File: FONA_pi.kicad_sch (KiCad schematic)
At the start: 6 parts, among them J1 Conn_01x20_Socket, J2 Conn_02x20_Odd_Even, J3 Conn_01x20_Socket, J5 Conn_01x20_Socket, J6 Conn_01x20_Socket, J8 Conn_01x20_Socket

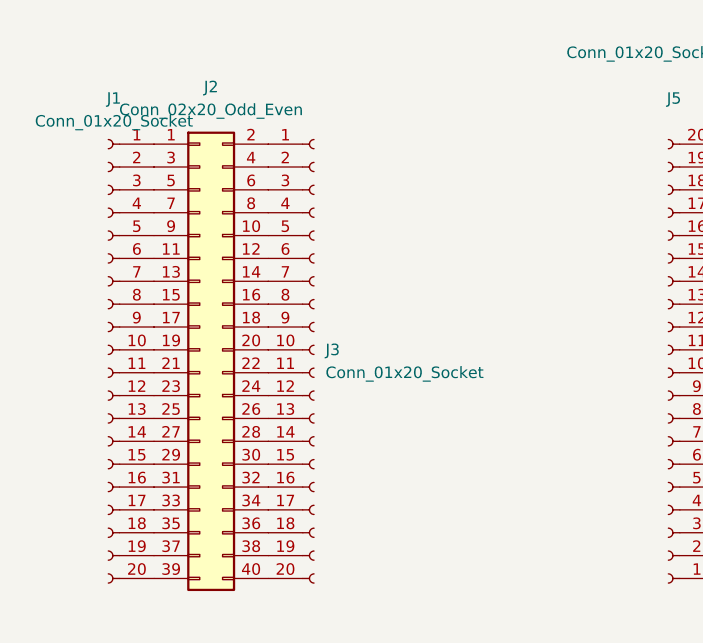
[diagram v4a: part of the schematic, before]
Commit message: Added more rows of holes to connect to Pi
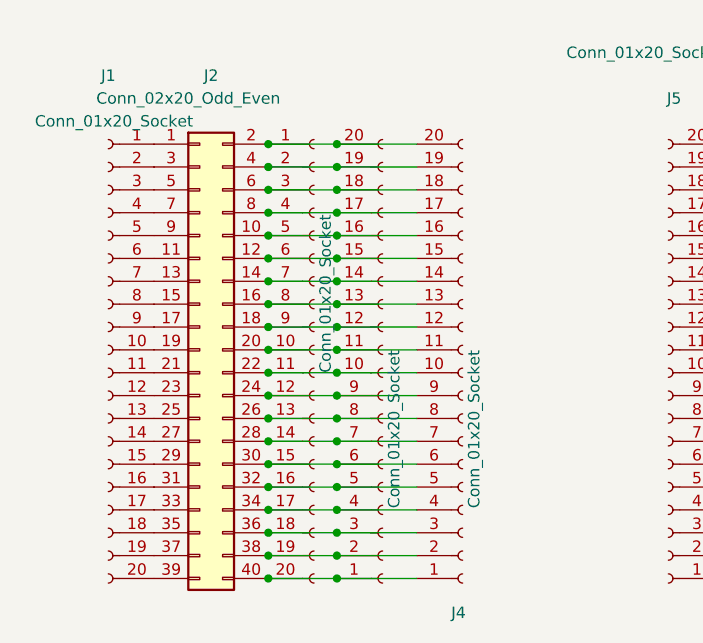
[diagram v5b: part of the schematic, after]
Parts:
- added J4, J7: Conn_01x20_Socket, Connector_PinHeader_2.54mm:PinHeader_1x20_P2.54mm_Vertical, symbol Connector:Conn_01x20_Socket
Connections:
- net at J2.10 (Pin_10), J3.5 (Pin_5): now also J4.16 (Pin_16), J7.16 (Pin_16)
- net at J2.12 (Pin_12), J3.6 (Pin_6): now also J4.15 (Pin_15), J7.15 (Pin_15)
- net at J2.14 (Pin_14), J3.7 (Pin_7): now also J4.14 (Pin_14), J7.14 (Pin_14)
- net at J2.16 (Pin_16), J3.8 (Pin_8): now also J4.13 (Pin_13), J7.13 (Pin_13)
- net at J2.18 (Pin_18), J3.9 (Pin_9): now also J4.12 (Pin_12), J7.12 (Pin_12)
- net at J2.2 (Pin_2), J3.1 (Pin_1): now also J4.20 (Pin_20), J7.20 (Pin_20)
- net at J2.20 (Pin_20), J3.10 (Pin_10): now also J4.11 (Pin_11), J7.11 (Pin_11)
- net at J2.22 (Pin_22), J3.11 (Pin_11): now also J4.10 (Pin_10), J7.10 (Pin_10)
- net at J2.24 (Pin_24), J3.12 (Pin_12): now also J4.9 (Pin_9), J7.9 (Pin_9)
- net at J2.26 (Pin_26), J3.13 (Pin_13): now also J4.8 (Pin_8), J7.8 (Pin_8)
- net at J2.28 (Pin_28), J3.14 (Pin_14): now also J4.7 (Pin_7), J7.7 (Pin_7)
- net at J2.30 (Pin_30), J3.15 (Pin_15): now also J4.6 (Pin_6), J7.6 (Pin_6)
- net at J2.32 (Pin_32), J3.16 (Pin_16): now also J4.5 (Pin_5), J7.5 (Pin_5)
- net at J2.34 (Pin_34), J3.17 (Pin_17): now also J4.4 (Pin_4), J7.4 (Pin_4)
- net at J2.36 (Pin_36), J3.18 (Pin_18): now also J4.3 (Pin_3), J7.3 (Pin_3)
- net at J2.38 (Pin_38), J3.19 (Pin_19): now also J4.2 (Pin_2), J7.2 (Pin_2)
- net at J2.4 (Pin_4), J3.2 (Pin_2): now also J4.19 (Pin_19), J7.19 (Pin_19)
- net at J2.40 (Pin_40), J3.20 (Pin_20): now also J4.1 (Pin_1), J7.1 (Pin_1)
- net at J2.6 (Pin_6), J3.3 (Pin_3): now also J4.18 (Pin_18), J7.18 (Pin_18)
- net at J2.8 (Pin_8), J3.4 (Pin_4): now also J4.17 (Pin_17), J7.17 (Pin_17)

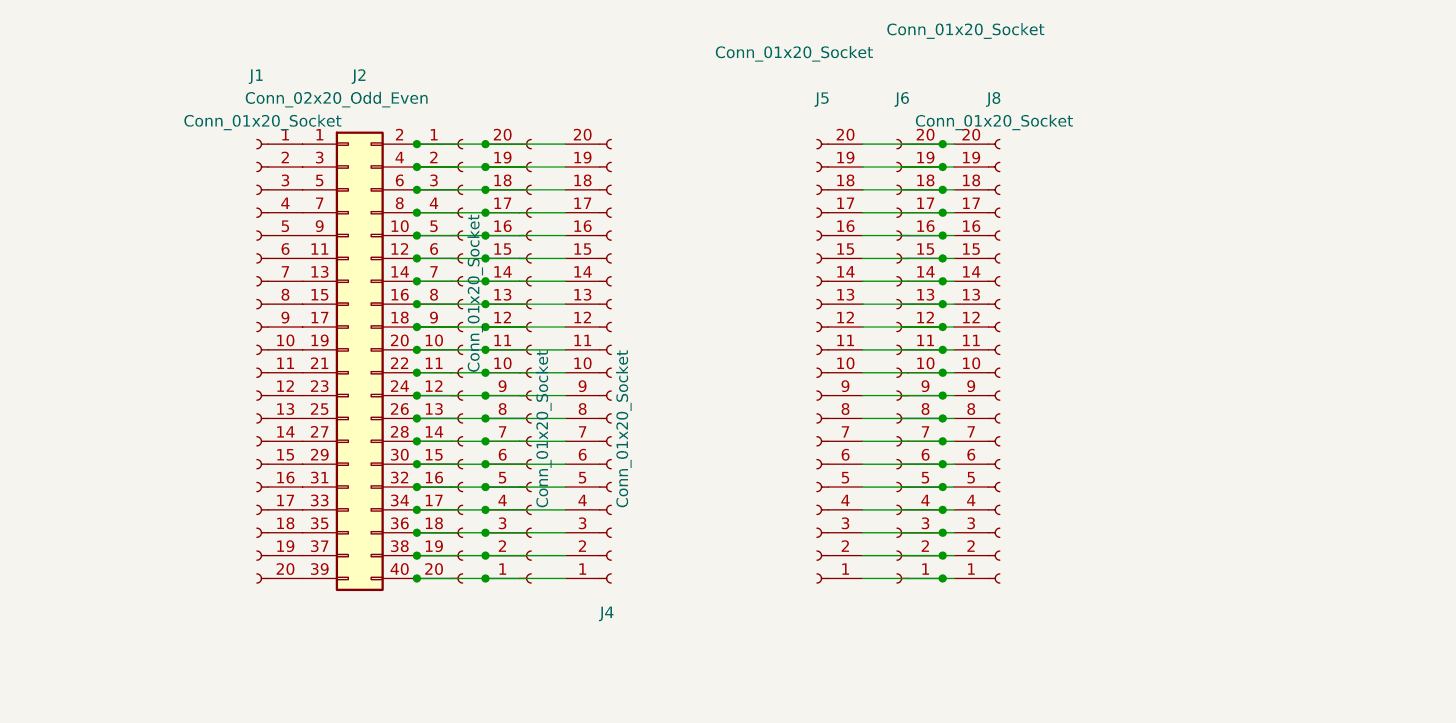
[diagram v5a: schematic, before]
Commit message: flipped RPi orientation on schematic.  Added three 3mm LEDs with resistors on sch and pcb.  Wired up with traces
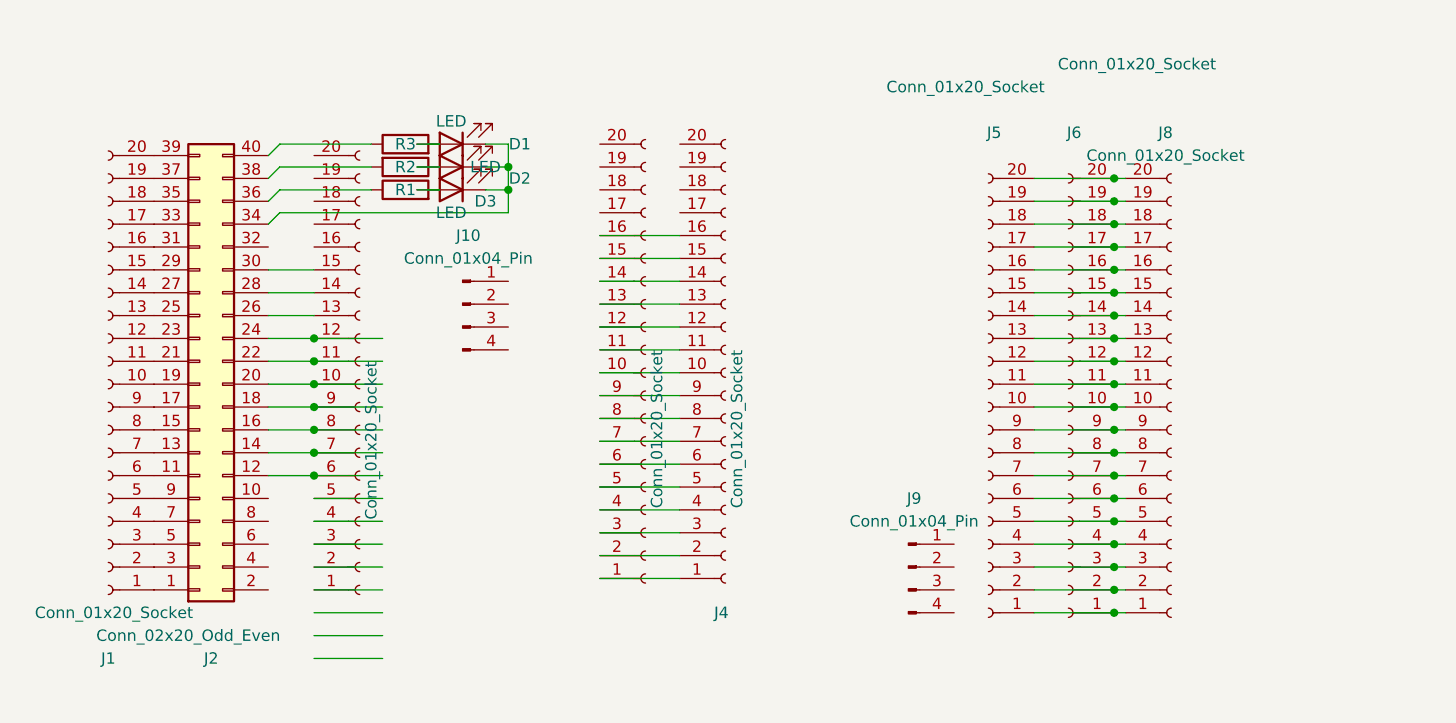
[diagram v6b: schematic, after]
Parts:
- added D1, D2, D3: LED, LED_THT:LED_D3.0mm, symbol Device:LED
- added J10, J9: Conn_01x04_Pin, symbol Connector:Conn_01x04_Pin
- added R1, R2, R3: R, Resistor_THT:R_Axial_DIN0207_L6.3mm_D2.5mm_P7.62mm_Horizontal, symbol Device:R
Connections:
- net at J4.1 (Pin_1), J7.1 (Pin_1): no longer J2.40 (Pin_40), J3.20 (Pin_20)
- net at J4.10 (Pin_10), J7.10 (Pin_10): no longer J2.22 (Pin_22), J3.11 (Pin_11)
- net at J4.11 (Pin_11), J7.11 (Pin_11): no longer J2.20 (Pin_20), J3.10 (Pin_10)
- net at J4.12 (Pin_12), J7.12 (Pin_12): no longer J2.18 (Pin_18), J3.9 (Pin_9)
- net at J4.13 (Pin_13), J7.13 (Pin_13): no longer J2.16 (Pin_16), J3.8 (Pin_8)
- net at J4.14 (Pin_14), J7.14 (Pin_14): no longer J2.14 (Pin_14), J3.7 (Pin_7)
- net at J4.15 (Pin_15), J7.15 (Pin_15): no longer J2.12 (Pin_12), J3.6 (Pin_6)
- net at J4.16 (Pin_16), J7.16 (Pin_16): no longer J2.10 (Pin_10), J3.5 (Pin_5)
- net at J4.2 (Pin_2), J7.2 (Pin_2): no longer J2.38 (Pin_38), J3.19 (Pin_19)
- net at J4.3 (Pin_3), J7.3 (Pin_3): no longer J2.36 (Pin_36), J3.18 (Pin_18)
- net at J4.4 (Pin_4), J7.4 (Pin_4): no longer J2.34 (Pin_34), J3.17 (Pin_17)
- net at J4.5 (Pin_5), J7.5 (Pin_5): no longer J2.32 (Pin_32), J3.16 (Pin_16)
- net at J4.6 (Pin_6), J7.6 (Pin_6): no longer J2.30 (Pin_30), J3.15 (Pin_15)
- net at J4.7 (Pin_7), J7.7 (Pin_7): no longer J2.28 (Pin_28), J3.14 (Pin_14)
- net at J4.8 (Pin_8), J7.8 (Pin_8): no longer J2.26 (Pin_26), J3.13 (Pin_13)
- net at J4.9 (Pin_9), J7.9 (Pin_9): no longer J2.24 (Pin_24), J3.12 (Pin_12)
- new net: D2.2 (A), R2.1
- new net: J2.38 (Pin_38), R2.2
- new net: J2.12 (Pin_12), J3.6 (Pin_6)
- new net: J2.14 (Pin_14), J3.7 (Pin_7)
- new net: J2.16 (Pin_16), J3.8 (Pin_8)
- new net: J2.18 (Pin_18), J3.9 (Pin_9)
- new net: J2.20 (Pin_20), J3.10 (Pin_10)
- new net: J2.22 (Pin_22), J3.11 (Pin_11)
- new net: J2.24 (Pin_24), J3.12 (Pin_12)
- new net: J2.26 (Pin_26), J3.13 (Pin_13)
- new net: J2.28 (Pin_28), J3.14 (Pin_14)
- new net: J2.30 (Pin_30), J3.15 (Pin_15)
- new net: D1.1 (K), D2.1 (K), D3.1 (K), J2.34 (Pin_34)
- new net: J2.36 (Pin_36), R1.1
- new net: J2.40 (Pin_40), R3.1
- new net: D1.2 (A), R3.2
- new net: D3.2 (A), R1.2
- now unconnected: J2.2 (Pin_2), J2.4 (Pin_4), J2.6 (Pin_6), J2.8 (Pin_8), J3.1 (Pin_1), J3.2 (Pin_2), J3.3 (Pin_3), J3.4 (Pin_4), J4.17 (Pin_17), J4.18 (Pin_18), J4.19 (Pin_19), J4.20 (Pin_20), J7.17 (Pin_17), J7.18 (Pin_18), J7.19 (Pin_19), J7.20 (Pin_20)
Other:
- moved on the sheet: J1, J2, J4, J5, J6, J8

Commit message: Hooked up JST-XH connectors, resistors
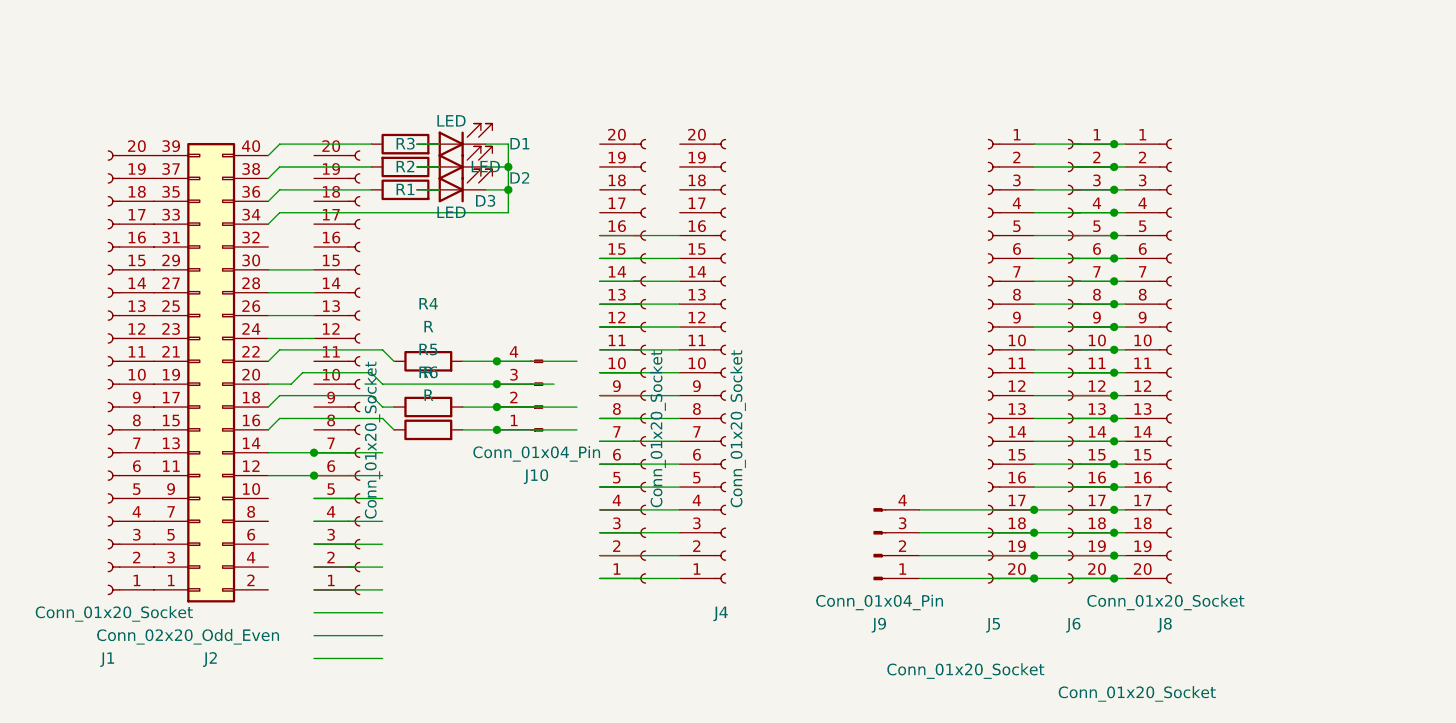
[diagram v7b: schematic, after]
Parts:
- added R4, R5, R6: R, Resistor_THT:R_Axial_DIN0207_L6.3mm_D2.5mm_P7.62mm_Horizontal, symbol Device:R
- J10, J9: footprint (none) -> Connector_JST:JST_XH_B4B-XH-A_1x04_P2.50mm_Vertical
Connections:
- net at J5.17 (Pin_17), J6.17 (Pin_17), J8.17 (Pin_17): now also J9.4 (Pin_4)
- net at J5.18 (Pin_18), J6.18 (Pin_18), J8.18 (Pin_18): now also J9.3 (Pin_3)
- net at J5.19 (Pin_19), J6.19 (Pin_19), J8.19 (Pin_19): now also J9.2 (Pin_2)
- net at J5.20 (Pin_20), J6.20 (Pin_20), J8.20 (Pin_20): now also J9.1 (Pin_1)
- net at J2.16 (Pin_16): now also R6.1; no longer J3.8 (Pin_8)
- net at J2.18 (Pin_18): now also R5.1; no longer J3.9 (Pin_9)
- net at J2.20 (Pin_20): now also J10.3 (Pin_3); no longer J3.10 (Pin_10)
- net at J2.22 (Pin_22): now also R4.1; no longer J3.11 (Pin_11)
- net at J10.1 (Pin_1): now also R6.2
- net at J10.2 (Pin_2): now also R5.2
- net at J10.4 (Pin_4): now also R4.2
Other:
- moved on the sheet: J10, J5, J6, J8, J9

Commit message: Flipped RPi pins.  Added silkscreen labels for pins.  Connected wires and tracks
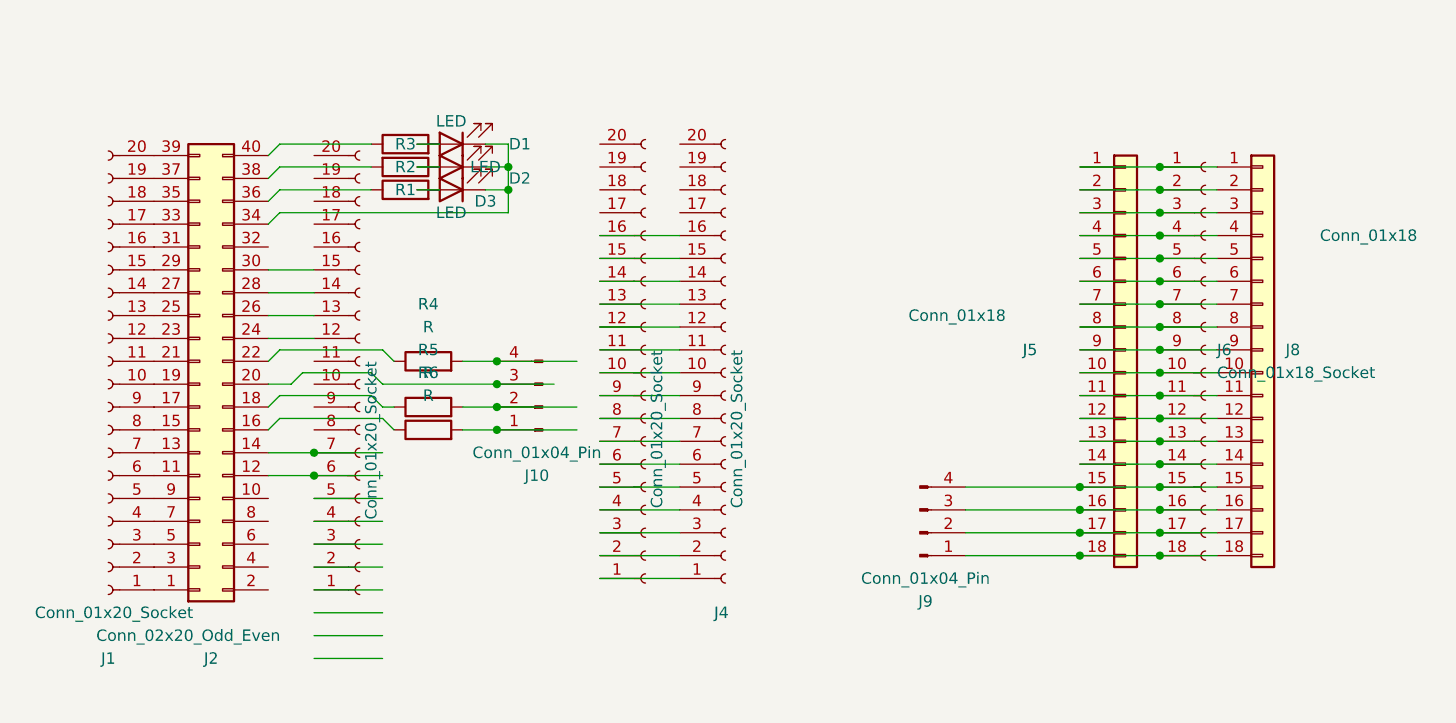
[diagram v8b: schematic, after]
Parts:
- removed J5, J6, J8: Conn_01x20_Socket, Connector_PinSocket_2.54mm:PinSocket_1x20_P2.54mm_Vertical, symbol Connector:Conn_01x20_Socket
- added J5, J8: Conn_01x18, Connector_PinSocket_2.54mm:PinSocket_1x18_P2.54mm_Vertical, symbol Connector_Generic:Conn_01x18
- added J6: Conn_01x18_Socket, Connector_PinSocket_2.54mm:PinSocket_1x18_P2.54mm_Vertical, symbol Connector:Conn_01x18_Socket
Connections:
- net at J9.4 (Pin_4): now also J5.15 (Pin_15), J6.15 (Pin_15), J8.15 (Pin_15)
- net at J9.3 (Pin_3): now also J5.16 (Pin_16), J6.16 (Pin_16), J8.16 (Pin_16)
- net at J9.2 (Pin_2): now also J5.17 (Pin_17), J6.17 (Pin_17), J8.17 (Pin_17)
- net at J9.1 (Pin_1): now also J5.18 (Pin_18), J6.18 (Pin_18), J8.18 (Pin_18)
- new net: J5.1 (Pin_1), J6.1 (Pin_1), J8.1 (Pin_1)
- new net: J5.10 (Pin_10), J6.10 (Pin_10), J8.10 (Pin_10)
- new net: J5.11 (Pin_11), J6.11 (Pin_11), J8.11 (Pin_11)
- new net: J5.12 (Pin_12), J6.12 (Pin_12), J8.12 (Pin_12)
- new net: J5.13 (Pin_13), J6.13 (Pin_13), J8.13 (Pin_13)
- new net: J5.14 (Pin_14), J6.14 (Pin_14), J8.14 (Pin_14)
- new net: J5.2 (Pin_2), J6.2 (Pin_2), J8.2 (Pin_2)
- new net: J5.3 (Pin_3), J6.3 (Pin_3), J8.3 (Pin_3)
- new net: J5.4 (Pin_4), J6.4 (Pin_4), J8.4 (Pin_4)
- new net: J5.5 (Pin_5), J6.5 (Pin_5), J8.5 (Pin_5)
- new net: J5.6 (Pin_6), J6.6 (Pin_6), J8.6 (Pin_6)
- new net: J5.7 (Pin_7), J6.7 (Pin_7), J8.7 (Pin_7)
- new net: J5.8 (Pin_8), J6.8 (Pin_8), J8.8 (Pin_8)
- new net: J5.9 (Pin_9), J6.9 (Pin_9), J8.9 (Pin_9)
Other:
- moved on the sheet: J9
